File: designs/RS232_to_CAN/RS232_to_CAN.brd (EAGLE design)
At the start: 160 x 100 mm, 53 parts, among them IC1 STM32F042K6T6TR, IC2 TJA1050T_CM,118, IC3 MAX232DRG4, IC4 FT232RL-TUBE, J1 FTSH-107-01-L-DV-K-A, J2 K202XHT-E9S-N, J3 K202XHT-E9S-N, J4 PJ-002AH-SMT-TR, J5 10118192-0001LF, Q1 FDN5632N-F085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

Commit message: added brd laxout
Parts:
- removed J1: FTSH-107-01-L-DV-K-A, MouserUseful:FTSH10701LDVKA
- removed S1: PTS526_SM15_SMTR2_LFS, MouserUseful:PTS526SM15SMTR2LFS
- added PRGM: FTSH-107-01-L-DV-K-A, MouserUseful:FTSH10701LDVKA
- added R12, R13: (no value), CommonParts:R0805
- added RST: PTS526_SM15_SMTR2_LFS, MouserUseful:PTS526SM15SMTR2LFS
- moved LED6 148.7 mm to (69.8, 77.5), turned to 90 degrees
- moved R7 128.8 mm to (54.6, 76.2), turned to 90 degrees
- moved C3 128.8 mm to (61.0, 43.2), turned to 180 degrees
- moved R1 126.1 mm to (45.7, 34.3), turned to 180 degrees
- moved C2 122.2 mm to (61.0, 47.0)
- moved C1 115.6 mm to (61.0, 52.1)
- moved SJ2 111.4 mm to (30.5, 25.4)
- moved LED2 110.3 mm to (47.0, 43.2)
- moved SJ1 109.6 mm to (30.5, 20.3)
- moved R10 107.3 mm to (69.8, 66.0), turned to 90 degrees
- moved C17 105.6 mm to (64.8, 61.0), turned to 180 degrees
- moved LED1 102.4 mm to (47.0, 50.8)
- moved R9 101.7 mm to (69.8, 72.4), turned to 90 degrees
- moved LED4 99.9 mm to (25.4, 50.8)
- moved C16 98.2 mm to (50.8, 63.5), turned to 270 degrees
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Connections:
- new net N$22: R12.2
- new net N$23: R13.2
- net 3.3V: now also PRGM.3; no longer J1.3
- net 5V: no longer J4.1, J4.2
- net AGND: now also PRGM.11, PRGM.5, PRGM.7, Q1.2, Q2.2, RST.1, RST.2; no longer J1.11, J1.5, J1.7, LED1.C, LED2.C, S1.1, S1.2
- net IN: now also J4.1, J4.2, LED1.C, LED2.C
- net N$13: now also R12.1; no longer Q2.2
- net N$8: now also R13.1; no longer Q1.2
- net NRST: now also PRGM.12, RST.3, RST.4; no longer J1.12, S1.3, S1.4
- net SWCLK: now also PRGM.6; no longer J1.6
- net SWIDO: now also PRGM.4; no longer J1.4
- net UART1_RX: now also PRGM.13; no longer J1.13
- net UART1_TX: now also PRGM.14; no longer J1.14
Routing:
- net AGND: track 0.00 -> 419.7 mm, vias 0 -> 17
- net 5V: track 0.00 -> 231.5 mm, vias 0 -> 12
- net 3.3V: track 0.00 -> 127.0 mm, vias 0 -> 10
- net IN: track 0.00 -> 113.2 mm, vias 0 -> 9
- net SHIELD: track 0.00 -> 106.3 mm, vias 0 -> 6
- net UART1_RX: track 0.00 -> 85.5 mm, vias 0 -> 5
- net UART1_TX: track 0.00 -> 75.3 mm, vias 0 -> 6
- net TXD: track 0.00 -> 56.5 mm, vias 0 -> 2
- net RI#: track 0.00 -> 50.7 mm, vias 0 -> 2
- net PWERN#: track 0.00 -> 50.4 mm, vias 0 -> 2
- net RTS#: track 0.00 -> 48.9 mm
- net NRST: track 0.00 -> 48.3 mm, vias 0 -> 2
- net RXD: track 0.00 -> 47.3 mm, vias 0 -> 2
- net T2OUT: track 0.00 -> 43.0 mm, vias 0 -> 4
- net CTS#: track 0.00 -> 40.7 mm
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- added copper zone on layer 1, net AGND
- added copper zone on layer 16, net AGND
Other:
- board size 160 x 100 mm -> 77.5 x 83.8 mm
- board text added: "CAN"
- board text added: "FT232"
- board text added: "Logic"
- board text added: "MAX232"
- board text added: "Power"
- board text added: "RS232 to CAN 1.0 Moritz Bösenberg"

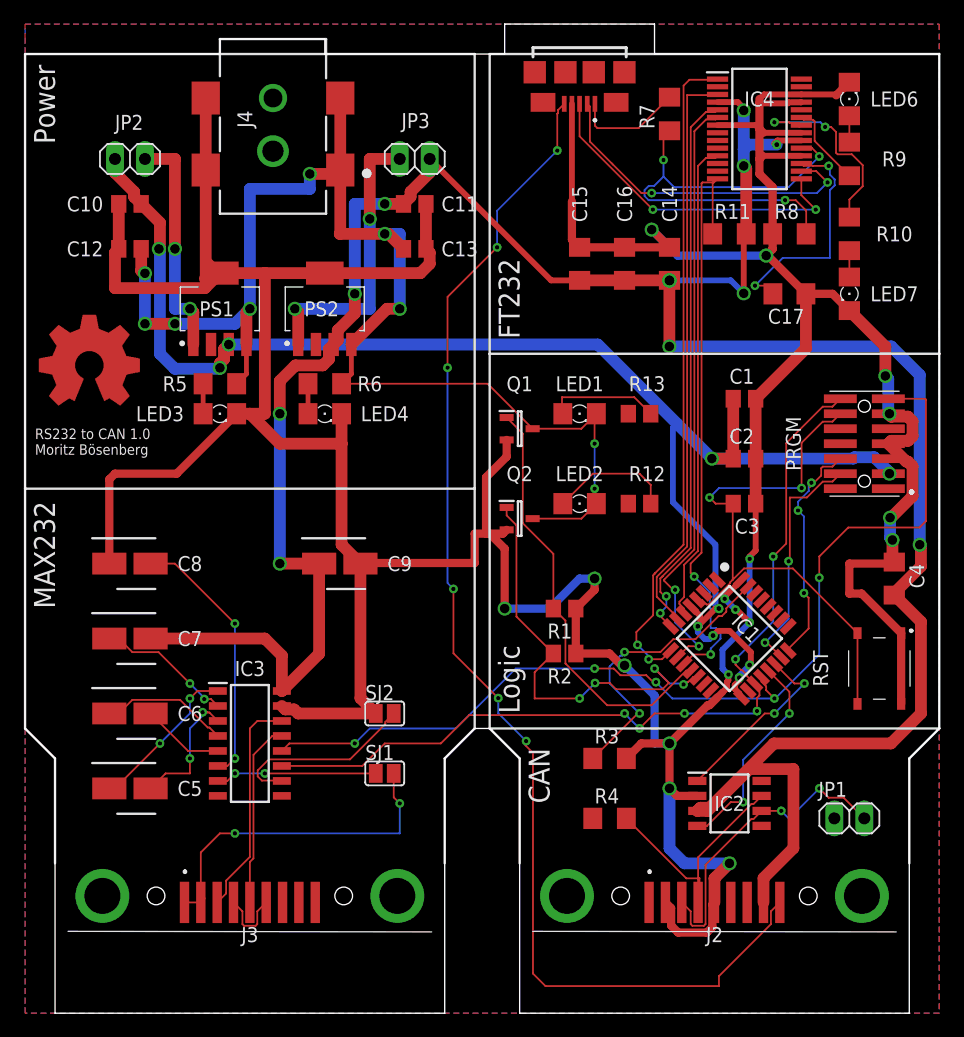
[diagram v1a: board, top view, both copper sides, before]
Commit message: added battery loader + 3.3V regulator
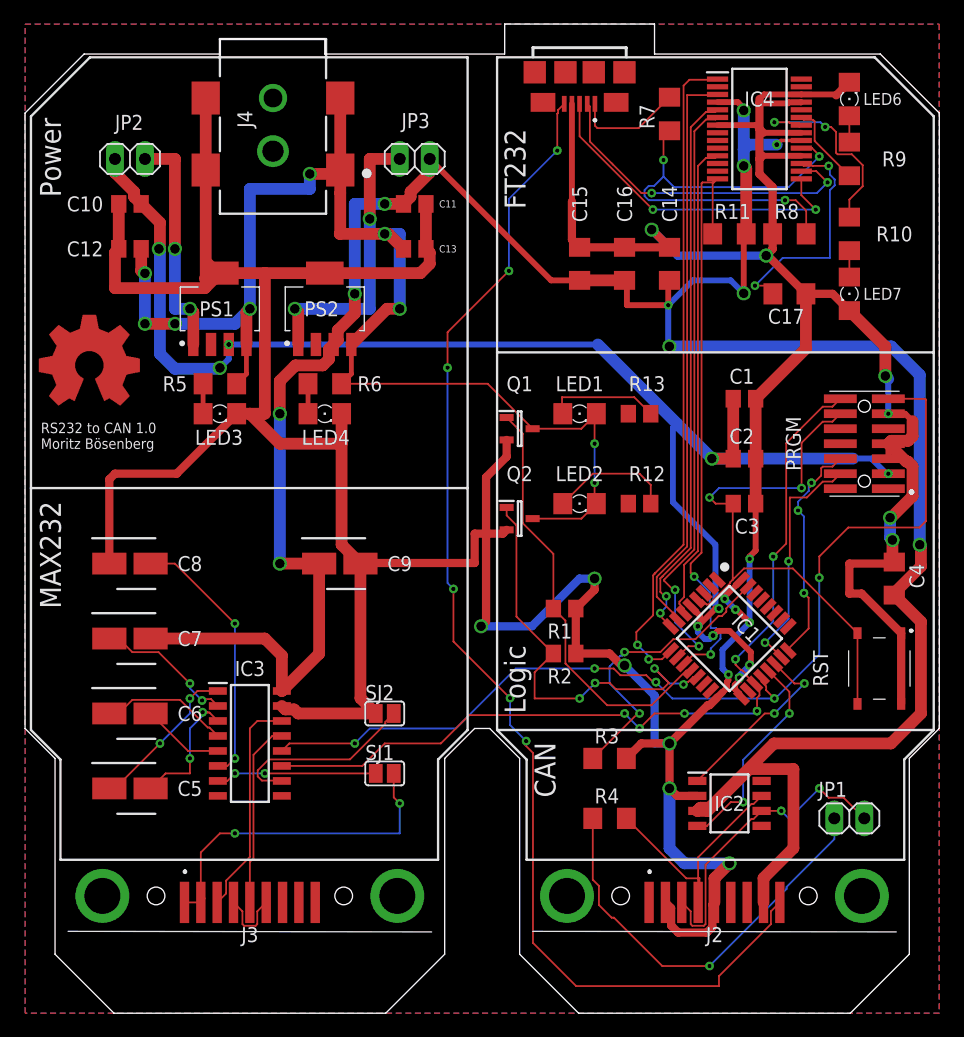
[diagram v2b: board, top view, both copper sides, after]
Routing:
- net N$2: track 0.00 -> 36.0 mm, vias 0 -> 1
- net AGND: track 419.7 -> 424.3 mm
- net 5V: track 231.5 -> 234.0 mm, vias 12 -> 11
- net IN: track 113.2 -> 114.9 mm
- net SHIELD: track 106.3 -> 104.7 mm
- net 3.3V: track 127.0 -> 126.7 mm, vias 10 -> 11
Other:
- outline, holes or cut-outs redrawn
